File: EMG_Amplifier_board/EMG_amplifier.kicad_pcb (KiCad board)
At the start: 2 copper layers, 50.1 x 39.8 mm, 52 parts, among them J1 Conn_01x04_Socket, J2 Conn_01x04_Pin, J3 Conn_01x06_Pin, J4 Conn_01x06_Socket, J5 Conn_01x04_Pin, J6 Conn_01x01_Pin, U1 LPV821DBVR, U2 INA333xxDGK, U3 LPV821DBVR, U5 LPV821DBVR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

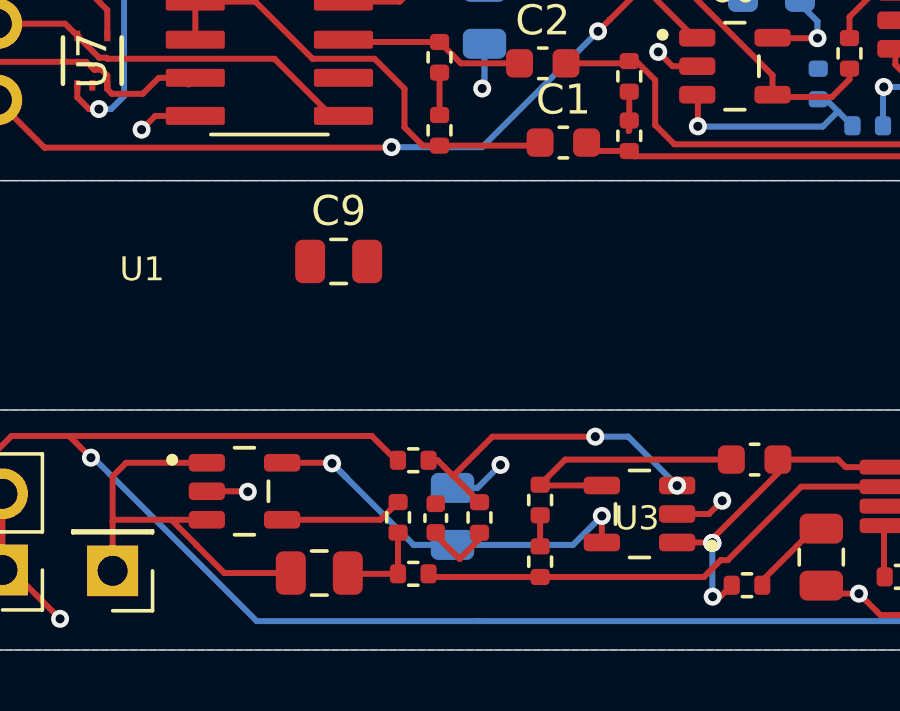
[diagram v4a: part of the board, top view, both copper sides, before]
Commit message: use one C10 capacitor instead of both C9 and C10
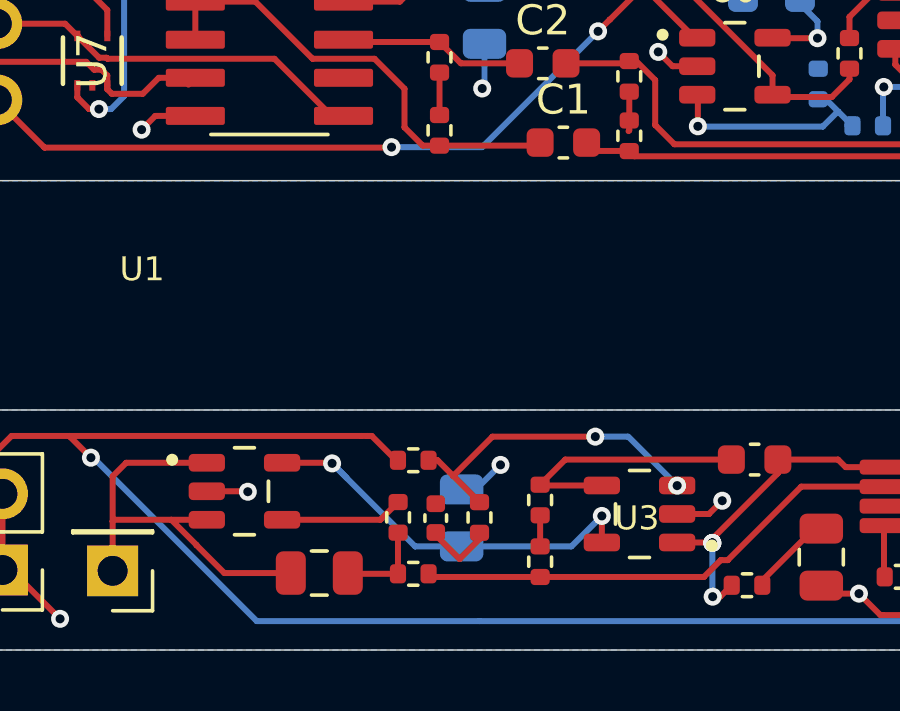
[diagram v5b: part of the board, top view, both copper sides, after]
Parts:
- removed C9: 0.1uF, Capacitor_SMD:C_0805_2012Metric
- moved C10 0.31 mm to (76.9, 117.9)
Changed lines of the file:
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@@
 		)
 	)
-	(footprint "Capacitor_SMD:C_0805_2012Metric"
-		(layer "F.Cu")
-		(at 72.7608 109.3724)
-		(descr "Capacitor SMD 0805 (2012 Metric), square (rectangular) end terminal, IPC_7351 nominal, (Body size source: IPC-SM-782 page 76, https://www.pcb-3d.com/wordpress/wp-content/uploads/ipc-sm-782a_amendment_1_and_2.pdf, https://docs.google.com/spreadsheets/d/1BsfQQcO9C6DZCsRaXUlFlo91Tg2WpOkGARC1WS5S8t0/edit?usp=sharing), generated with kicad-footprint-generator")
-		(tags "capacitor")
-		(property "Reference" "C9"
-			(at 0 -1.68 0)
-			(layer "F.SilkS")
-			(effects
-				(font
-					(size 1 1)
-					(thickness 0.15)
-				)
-			)
-		)
-		(property "Value" "0.1uF"
-			(at 0 1.68 0)
-			(layer "F.Fab")
-			(effects
-				(font
-					(size 1 1)
-					(thickness 0.15)
-				)
-			)
-		)
-		(property "Footprint" "Capacitor_SMD:C_0805_2012Metric"
-			(at 0 0 0)
-			(unlocked yes)
-			(layer "F.Fab")
-			(hide yes)
-			(effects
-				(font
-					(size 1.27 1.27)
-					(thickness 0.15)
-				)
-			)
-		)
-		(property "Datasheet" ""
-			(at 0 0 0)
-			(unlocked yes)
-			(layer "F.Fab")
-			(hide yes)
-			(effects
-				(font
-					(size 1.27 1.27)
-					(thickness 0.15)
-				)
-			)
-		)
-		(property "Description" "Unpolarized capacitor, small symbol"
-			(at 0 0 0)
-			(unlocked yes)
-			(layer "F.Fab")
-			(hide yes)
-			(effects
-				(font
-					(size 1.27 1.27)
-					(thickness 0.15)
-				)
-			)
-		)
-		(property ki_fp_filters "C_*")
-		(sheetname "first_amp_stage")
-		(sheetfile "first_amp_stage.kicad_sch")
-		(attr smd)
-		(fp_line
-			(start -0.261252 -0.735)
-			(end 0.261252 -0.735)
-			(stroke
-				(width 0.12)
-				(type solid)
-			)
-			(layer "F.SilkS")
-		)
-		(fp_line
-			(start -0.261252 0.735)
-			(end 0.261252 0.735)
-			(stroke
-				(width 0.12)
-				(type solid)
-			)
-			(layer "F.SilkS")
-		)
-		(fp_line
-			(start -1.7 -0.98)
-			(end 1.7 -0.98)
-			(stroke
-				(width 0.05)
-				(type solid)
-			)
-			(layer "F.CrtYd")
-		)
-		(fp_line
-			(start -1.7 0.98)
-			(end -1.7 -0.98)
-			(stroke
-				(width 0.05)
-				(type solid)
-			)
-			(layer "F.CrtYd")
-		)
-		(fp_line
-			(start 1.7 -0.98)
-			(end 1.7 0.98)
-			(stroke
-				(width 0.05)
-				(type solid)
-			)
-			(layer "F.CrtYd")
-		)
-		(fp_line
-			(start 1.7 0.98)
-			(end -1.7 0.98)
-			(stroke
-				(width 0.05)
-				(type solid)
-			)
-			(layer "F.CrtYd")
-		)
-		(fp_line
-			(start -1 -0.625)
-			(end 1 -0.625)
-			(stroke
-				(width 0.1)
-				(type solid)
-			)
-			(layer "F.Fab")
-		)
-		(fp_line
-			(start -1 0.625)
-			(end -1 -0.625)
-			(stroke
-				(width 0.1)
-				(type solid)
-			)
-			(layer "F.Fab")
-		)
-		(fp_line
-			(start 1 -0.625)
-			(end 1 0.625)
-			(stroke
-				(width 0.1)
-				(type solid)
-			)
-			(layer "F.Fab")
-		)
-		(fp_line
-			(start 1 0.625)
-			(end -1 0.625)
-			(stroke
-				(width 0.1)
-				(type solid)
-			)
-			(layer "F.Fab")
-		)
-		(fp_text user "${REFERENCE}"
-			(at 0 0 0)
-			(layer "F.Fab")
-			(effects
-				(font
-					(size 0.5 0.5)
-					(thickness 0.08)
-				)
-			)
-		)
-		(pad "1" smd roundrect
-			(at -0.95 0)
-			(size 1 1.45)
-			(layers "F.Cu" "F.Paste" "F.Mask")
-			(roundrect_rratio 0.25)
-			(net 34 "+1V8")
-			(pintype "passive")
-		)
-		(pad "2" smd roundrect
-			(at 0.95 0)
-			(size 1 1.45)
-			(layers "F.Cu" "F.Paste" "F.Mask")
-			(roundrect_rratio 0.25)
-			(net 1 "GND")
-			(pintype "passive")
-		)
-		(model "${KICAD8_3DMODEL_DIR}/Capacitor_SMD.3dshapes/C_0805_2012Metric.wrl"
-			(offset
-				(xyz 0 0 0)
-			)
-			(scale
-				(xyz 1 1 1)
-			)
-			(rotate
-				(xyz 0 0 0)
-			)
-		)
-	)
 	(footprint "TLV8542DR:SOIC127P599X175-8N"
 		(layer "F.Cu")
@@
 	(footprint "Capacitor_SMD:C_0805_2012Metric"
 		(layer "B.Cu")
-		(at 76.5556 117.8712 90)
+		(at 76.8604 117.922 90)
 		(descr "Capacitor SMD 0805 (2012 Metric), square (rectangular) end terminal, IPC_7351 nominal, (Body size source: IPC-SM-782 page 76, https://www.pcb-3d.com/wordpress/wp-content/uploads/ipc-sm-782a_amendment_1_and_2.pdf, https://docs.google.com/spreadsheets/d/1BsfQQcO9C6DZCsRaXUlFlo91Tg2WpOkGARC1WS5S8t0/edit?usp=sharing), generated with kicad-footprint-generator")
 		(tags "capacitor")
@@
 			(at 0 1.68 90)
 			(layer "B.SilkS")
-			(hide yes)
 			(effects
 				(font
@@
 			(at 0 -1.68 90)
 			(layer "B.Fab")
-			(hide yes)
 			(effects
 				(font
@@
 	)
 	(segment
-		(start 96.734 119.3946)
-		(end 96.734 115.9236)
+		(start 76.8604 116.972)
+		(end 77.338 116.972)
 		(width 0.2)
 		(layer "B.Cu")
@@
 	)
 	(segment
-		(start 77.6224 103.5304)
-		(end 77.6224 102.1182)
+		(start 96.734 119.3946)
+		(end 96.734 115.9236)
 		(width 0.2)
 		(layer "B.Cu")
@@
 	)
 	(segment
-		(start 77.3888 116.9212)
-		(end 78.1558 116.1542)
+		(start 77.6224 103.5304)
+		(end 77.6224 102.1182)
 		(width 0.2)
 		(layer "B.Cu")
@@
 	)
 	(segment
+		(start 77.338 116.972)
+		(end 78.1558 116.1542)
+		(width 0.2)
+		(layer "B.Cu")
+		(net 1)
+	)
+	(segment
 		(start 95.8596 103.9114)
 		(end 95.8596 104.521)
@@
 	)
 	(segment
-		(start 76.5556 116.9212)
-		(end 77.3888 116.9212)
-		(width 0.2)
-		(layer "B.Cu")
-		(net 1)
-	)
-	(segment
 		(start 91.821 103.5558)
 		(end 92.5576 102.8192)
@@
 	)
 	(segment
-		(start 93.4262 119.761)
-		(end 93.4262 117.861)
+		(start 72.5424 116.1034)
+		(end 75.311 118.872)
 		(width 0.2)
 		(layer "B.Cu")
@@
 	)
 	(segment
-		(start 92.7608 121.3612)
-		(end 102.362 121.3612)
+		(start 93.4262 119.761)
+		(end 93.4262 117.861)
 		(width 0.2)
 		(layer "B.Cu")
@@
 	)
 	(segment
-		(start 75.2602 118.8212)
-		(end 72.5424 116.1034)
+		(start 92.7608 121.3612)
+		(end 102.362 121.3612)
 		(width 0.2)
 		(layer "B.Cu")
@@
 	)
 	(segment
-		(start 76.5556 118.8212)
-		(end 75.2602 118.8212)
-		(width 0.2)
-		(layer "B.Cu")
-		(net 34)
-	)
-	(segment
-		(start 80.5688 118.8212)
+		(start 80.518 118.872)
 		(end 81.534 117.856)
 		(width 0.2)
@@
 	)
 	(segment
-		(start 76.5556 118.8212)
-		(end 80.5688 118.8212)
+		(start 76.8604 118.872)
+		(end 80.518 118.872)
+		(width 0.2)
+		(layer "B.Cu")
+		(net 34)
+	)
+	(segment
+		(start 75.311 118.872)
+		(end 76.8604 118.872)
 		(width 0.2)
 		(layer "B.Cu")
@@
 		(width 0.2)
 		(layer "B.Cu")
+		(net 34)
+	)
+	(segment
+		(start 76.6318 118.8974)
+		(end 76.9366 119.2022)
+		(width 0.2)
+		(layer "B.Cu")

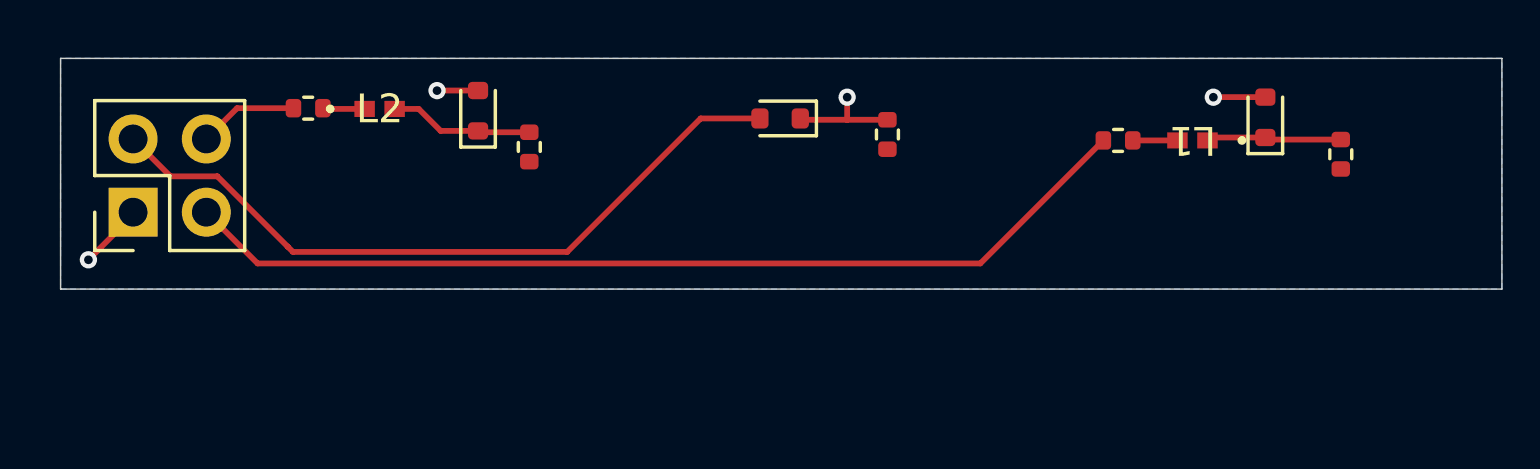
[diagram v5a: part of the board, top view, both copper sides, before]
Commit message: add vias for electrodes
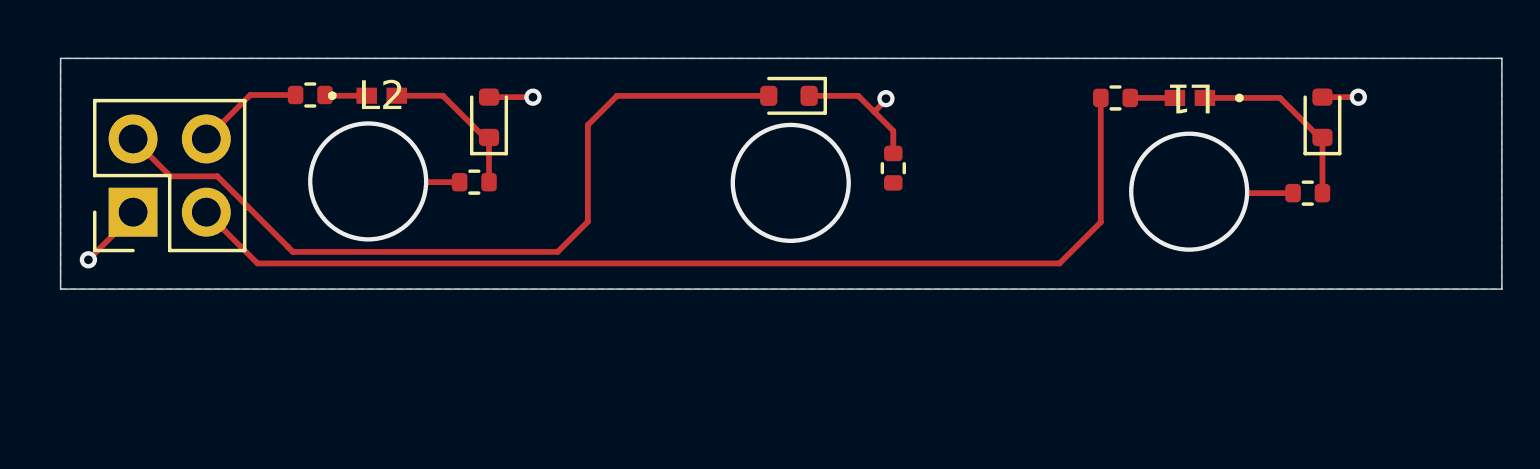
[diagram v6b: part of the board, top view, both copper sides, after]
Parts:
- moved R2 2.26 mm to (70.9, 86.8), turned to 0 degrees
- moved D1 1.98 mm to (100.3, 84.5)
- moved R1 1.77 mm to (99.8, 87.2), turned to 0 degrees
- moved L1 1.48 mm to (95.7, 83.9)
- moved R3 1.48 mm to (93.1, 83.9)
- moved R5 1.19 mm to (85.4, 86.3)
- moved D3 0.84 mm to (81.8, 83.8)
- moved L2 0.46 mm to (67.7, 83.8)
- moved R4 0.46 mm to (65.2, 83.8)
- moved D2 0.44 mm to (71.4, 84.5)
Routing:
- net input_E1: track 0.00 -> 3.62 mm, vias 0 -> 1
- net input_E2: track 0.00 -> 3.18 mm, vias 0 -> 1
- net /Electrode_Board/V_I1: track 33.6 -> 36.7 mm
- net /Electrode_Board/V_PR: track 25.3 -> 27.9 mm
- net Net-(D1-K): track 4.69 -> 6.58 mm
- net GND: track 59.6 -> 60.1 mm
- net input_ER: vias 0 -> 1

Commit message: minor link addition
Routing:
- net input_ER: track 0.00 -> 3.56 mm
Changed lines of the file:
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@@
 		(net 26)
+	)
+	(segment
+		(start 81.8388 86.8172)
+		(end 85.3948 86.8172)
+		(width 0.2)
+		(layer "F.Cu")
+		(net 27)
 	)
 	(via

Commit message: before working on one-sided design
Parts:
- removed J5: Conn_01x04_Pin, Connector_PinHeader_2.54mm:PinHeader_2x02_P2.54mm_Vertical
- removed J6: Conn_01x01_Pin, Connector_PinHeader_2.54mm:PinHeader_1x01_P2.54mm_Vertical
- added J7: Conn_01x06_Pin, Connector_PinHeader_2.54mm:PinHeader_2x03_P2.54mm_Vertical, F.Cu at (64.0, 105.0)
- J2: footprint Connector_PinSocket_2.54mm:PinSocket_2x02_P2.54mm_Vertical -> Connector_PinHeader_2.54mm:PinHeader_2x02_P2.54mm_Vertical
- moved C10 12.1 mm to (76.8, 105.9)
- moved C11 12.1 mm to (94.3, 107.7)
- moved C3 12.1 mm to (75.9, 105.9)
- moved C5 12.1 mm to (86.6, 103.9)
- moved C6 12.1 mm to (88.8, 107.2)
- moved J3 12.1 mm to (104.0, 107.5)
- moved R10 12.1 mm to (75.2, 107.7)
- moved R11 12.1 mm to (74.7, 105.8)
- moved R12 12.1 mm to (94.6, 107.8)
- moved R13 12.1 mm to (91.4, 107.8)
- moved R14 12.1 mm to (79.4, 105.3)
- moved R19 12.1 mm to (86.3, 108.1)
- moved R20 12.1 mm to (79.4, 107.3)
- moved R22 12.1 mm to (77.4, 105.8)
- moved U2 12.1 mm to (93.0, 105.1)
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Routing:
- net /Filtering_Board/V_PR: track 27.1 -> 31.8 mm
- net /Filtering_Board/V_I1: track 10.9 -> 8.40 mm
- net /Electrode_Board/V_I1: track 36.7 -> 38.9 mm
- net Net-(D1-K): track 6.58 -> 4.54 mm
- net Net-(L1-Pad2): track 1.55 -> 3.49 mm
- net Net-(D2-K): track 5.35 -> 7.26 mm
- net GND: track 60.1 -> 62.0 mm
- net +1V8: track 85.9 -> 84.2 mm
- net /Processing_Board/V_EMG_OUT: track 14.6 -> 13.1 mm
- net /Electrode_Board/V_PR: track 27.9 -> 26.8 mm
- net input_E1: track 3.62 -> 4.36 mm
- net input_E2: track 3.18 -> 3.87 mm
- net /Filtering_Board/+V_DD: track 74.8 -> 74.3 mm
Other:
- board size 50.1 x 39.8 mm -> 50 x 27.8 mm
